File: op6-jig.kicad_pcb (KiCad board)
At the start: 2 copper layers, 75 x 60.6 mm, 43 parts, among them J1 PHONE_TP_BREAKOUT, J2 JTAG_ATMEGA, J3 ATMEGA_MISC_GPIO, P1 USB_C_ATMEGA, P2 USB_C_PHONE, Q1 FQP27P06, SW1 SW_RESET, U1 ATMEGA32U4, U2 LSF0102YZTR, Y1 16MHz

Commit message: PCB: fix missing trace :C
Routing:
- net Net-(R11-Pad2): track 40.5 -> 52.7 mm
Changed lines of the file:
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@@
     (thickness 1.6)
     (drawings 84)
-    (tracks 705)
+    (tracks 709)
     (zones 0)
     (modules 43)
@@
   (segment (start 126.9264 107.409) (end 126.0799 106.5625) (width 0.25) (layer F.Cu) (net 29))
   (segment (start 126.0799 106.5625) (end 126.0799 106.4028) (width 0.25) (layer F.Cu) (net 29))
-  (via (at 126.0799 106.4028) (size 0.8) (layers F.Cu B.Cu) (net 29))
+  (via (at 126.0799 106.4028) (size 0.8) (layers F.Cu B.Cu) (net 29) (status 1000000))
   (via (at 97.5382 95.8206) (size 0.8) (layers F.Cu B.Cu) (net 29))
+  (segment (start 124.422099 104.744999) (end 126.0799 106.4028) (width 0.25) (layer B.Cu) (net 29))
+  (segment (start 121.525997 104.744999) (end 124.422099 104.744999) (width 0.25) (layer B.Cu) (net 29))
+  (segment (start 118.632998 101.852) (end 121.525997 104.744999) (width 0.25) (layer B.Cu) (net 29))
+  (segment (start 115.6776 101.852) (end 118.632998 101.852) (width 0.25) (layer B.Cu) (net 29))
   (via (at 89.4421 104.4869) (size 0.8) (layers F.Cu B.Cu) (net 30))
   (via (at 107.0924 118.3728) (size 0.8) (layers F.Cu B.Cu) (net 30))

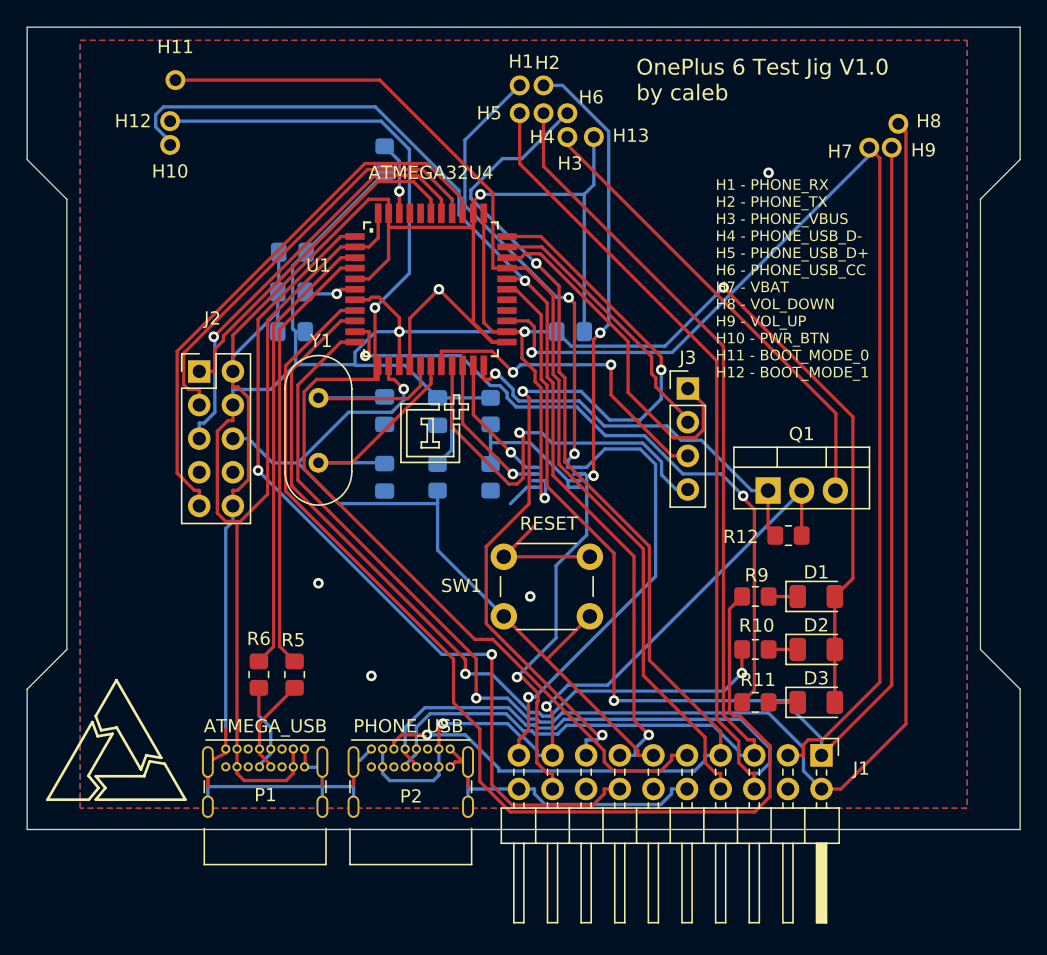
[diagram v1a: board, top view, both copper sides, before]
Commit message: pcb: rewire by hand
hah, i actually did it...

The PCB is now hand wired and muuuuuuuch better. This drops the USB pins
on the breakout header because they probably aren't needed and added too
much complexity to the traces.

Also replace the UART pinout with the 5v one on the Atmega side of the
level shifter rather than the 1.8v levels at the phone.
 * This would mean UART is borked unless you attach 5v to the Atmega USB
   port, maybe we want to power the level shifter with the phone vbus
   supply instead ?
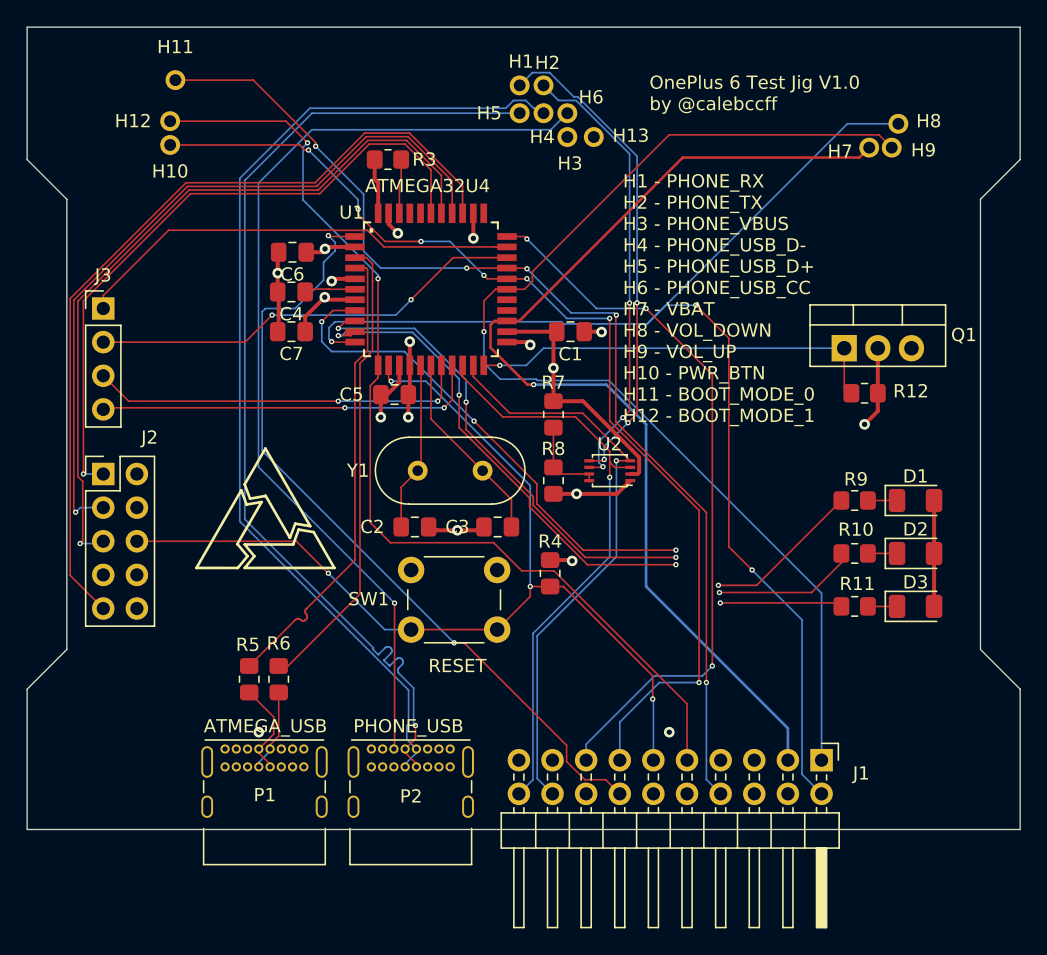
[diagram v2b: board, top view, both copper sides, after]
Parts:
- C1, C2, C3, C4, C5, C6, C7, R3, R4, R7, R8, U2: moved to F.Cu
- H4: value PHONE_USB_DN -> PHONE_USB_D-
- H5: value PHONE_USB_DP -> PHONE_USB_D+
- moved J3 44.6 mm to (77.8, 92.2)
- moved Q1 12.2 mm to (133.7, 95.2)
- moved R12 12.2 mm to (135.2, 98.7)
- moved R4 11.2 mm to (111.5, 112.2)
- moved J2 10.6 mm to (77.8, 104.8)
- moved D1 10.4 mm to (139.1, 106.8)
- moved D2 10.4 mm to (139.1, 110.8)
- moved D3 10.4 mm to (139.1, 114.8)
- moved R10 10.4 mm to (134.5, 110.8)
- moved R11 10.4 mm to (134.5, 114.8)
- moved R9 10.4 mm to (134.5, 106.8)
- moved C3 9.32 mm to (107.5, 108.8), turned to 180 degrees
- moved Y1 9.30 mm to (101.5, 104.5), turned to 0 degrees
- moved C2 9.08 mm to (101.3, 108.8), turned to 0 degrees
- moved SW1 7.07 mm to (101.0, 112.0)
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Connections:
- net Net-(P1-PadA6) renamed /ATMEGA_USB_D-
- net Net-(P1-PadA7) renamed /ATMEGA_USB_D+
- net Net-(R10-Pad2) renamed /LED_G_EN
- net Net-(R11-Pad2) renamed /LEG_B_EN
- net Net-(R5-Pad1) renamed /ATMEGA_USB_R_D-
- net Net-(R6-Pad1) renamed /ATMEGA_USB_R_D+
- net Net-(R9-Pad2) renamed /LED_R_EN
- H4 pad 1: PHONE_USB_DN -> PHONE_USB_D-
- H5 pad 1: PHONE_USB_DP -> PHONE_USB_D+
- J1 pad 18: PHONE_TX -> ATMEGA_TX
- J1 pad 19: PHONE_RX -> GND
- J1 pad 20: GND -> ATMEGA_RX
- J1 pad 5: PHONE_USB_DN -> Net-(J1-Pad5)
- J1 pad 6: PHONE_USB_DP -> Net-(J1-Pad6)
- J1 pad 7: PHONE_USB_CC -> Net-(J1-Pad7)
- P2 pad A6: PHONE_USB_DP -> PHONE_USB_D+
- P2 pad A7: PHONE_USB_DN -> PHONE_USB_D-
- P2 pad B6: PHONE_USB_DP -> PHONE_USB_D+
- P2 pad B7: PHONE_USB_DN -> PHONE_USB_D-
- U1 pad 20: Net-(U1-Pad20) -> ATMEGA_RX
- U1 pad 21: Net-(U1-Pad21) -> ATMEGA_TX
- U1 pad 31: Net-(J3-Pad1) -> Net-(J3-Pad2)
- U1 pad 32: Net-(J3-Pad2) -> Net-(J3-Pad1)
- U2 pad 3: Net-(U1-Pad20) -> ATMEGA_RX
- U2 pad 4: Net-(U1-Pad21) -> ATMEGA_TX
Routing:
- net /5v: track 214.2 -> 55.9 mm, vias 4 -> 6
- net GND: track 195.9 -> 47.7 mm, vias 6 -> 11
- net PHONE_USB_DP: track 95.7 -> 0.00 mm
- net PHONE_USB_DN: track 86.8 -> 0.00 mm
- net PHONE_USB_D+: track 0.00 -> 76.5 mm, vias 0 -> 1
- net PHONE_USB_D-: track 0.00 -> 76.2 mm
- net ATMEGA_RX: track 0.00 -> 44.7 mm, vias 0 -> 1
- net ATMEGA_TX: track 0.00 -> 44.5 mm, vias 0 -> 1
- net /LED_R_EN: track 84.9 -> 50.6 mm, vias 0 -> 4
- net PHONE_RX: track 68.9 -> 37.0 mm
- net PHONE_TX: track 61.6 -> 34.4 mm
- net JTAG_TMS: track 32.5 -> 56.8 mm
- net JTAG_TCK: track 26.2 -> 49.8 mm, vias 0 -> 1
- net JTAG_TCO: track 32.9 -> 55.8 mm, vias 0 -> 1
- net VOL_DOWN: track 119.4 -> 97.5 mm, vias 1 -> 3
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- added copper zone on In2.Cu, net /5v
- added copper zone on In1.Cu, net GND
- removed copper zone on B.Cu, net GND
- removed copper zone on F.Cu, net GND
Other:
- copper layers 2 -> 4
- net class Default: clearance 0.2 -> 0.15; trace_width 0.25 -> 0.127
- net class Power added: clearance 0.15, trace_width 0.3, via_dia 0.8, via_drill 0.4
- net class VBAT added: clearance 0.15, trace_width 0.2, via_dia 0.8, via_drill 0.4
- rule trace_clearance: 0.2 -> 0.15
- rule trace_min: 0.2 -> 0.1
- rule via_min_drill: 0.3 -> 0.2
- board text added: "OnePlus 6 Test Jig V1.0 by @calebccff"
- board text removed: "OnePlus 6 Test Jig V1.0 by caleb"

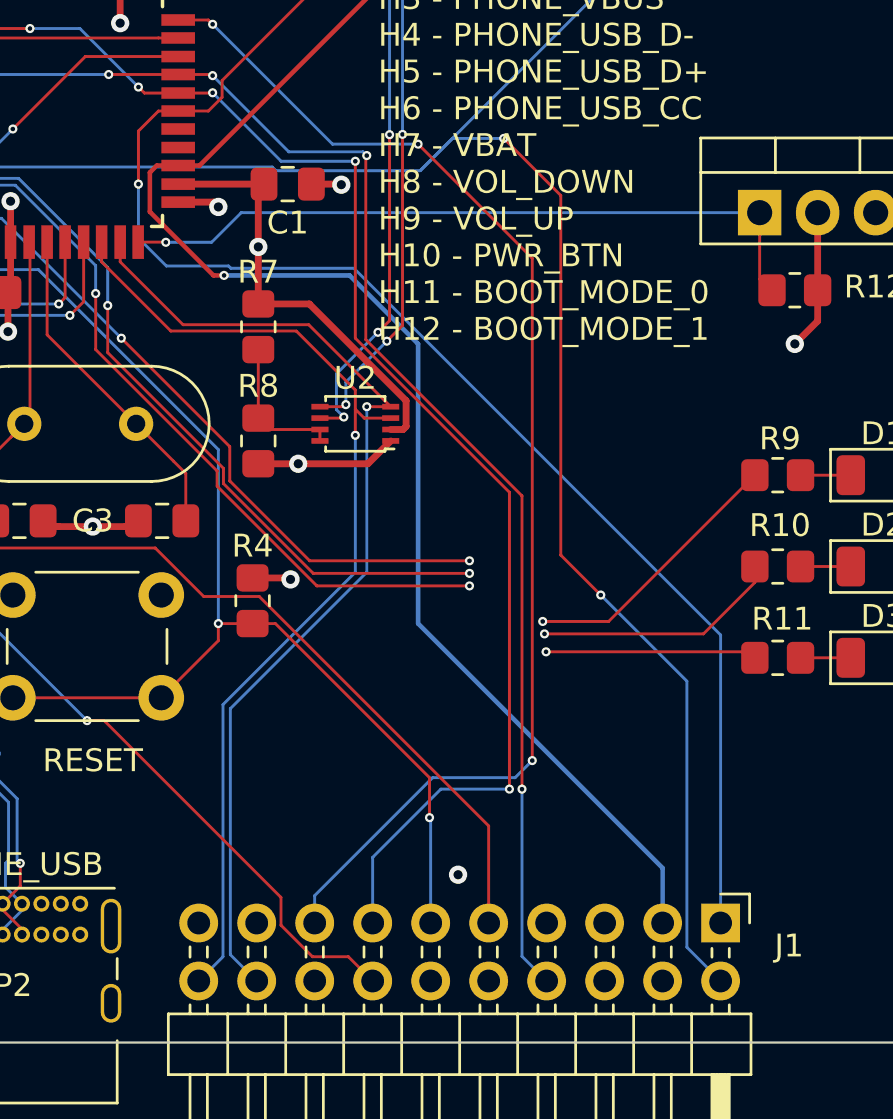
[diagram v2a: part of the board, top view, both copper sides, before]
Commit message: PCB: improve some routing
Less vias = more good :D
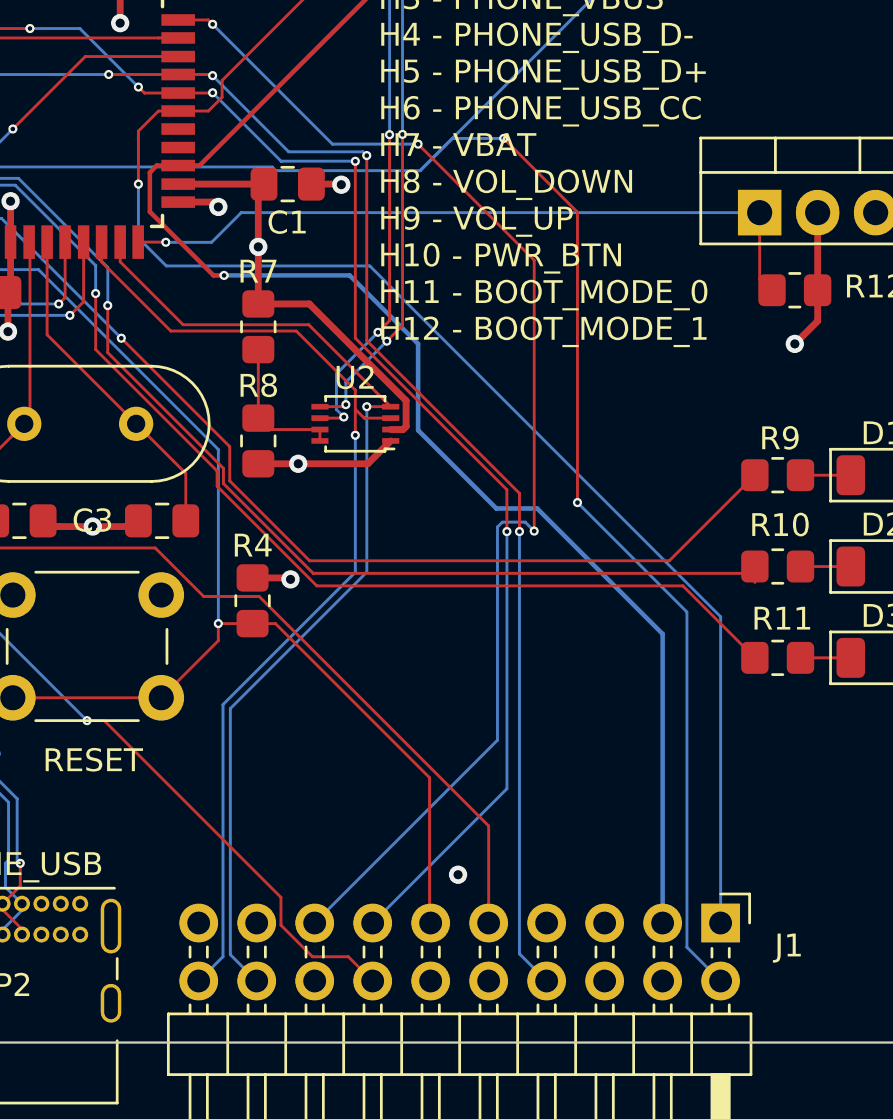
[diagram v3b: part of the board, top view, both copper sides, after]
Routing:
- net /LEG_B_EN: track 46.1 -> 51.0 mm, vias 4 -> 2
- net /LED_G_EN: track 47.7 -> 50.1 mm, vias 4 -> 2
- net /LED_R_EN: track 50.6 -> 52.6 mm, vias 4 -> 2
- net PWR_BTN: track 79.7 -> 77.8 mm
- net VBAT: track 79.8 -> 80.9 mm
- net HWB: track 55.0 -> 54.3 mm
- net RESET: vias 4 -> 3

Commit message: some minor fixes
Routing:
- net /5v: track 55.9 -> 69.1 mm, vias 6 -> 8
- net GND: track 47.7 -> 60.6 mm, vias 11 -> 10

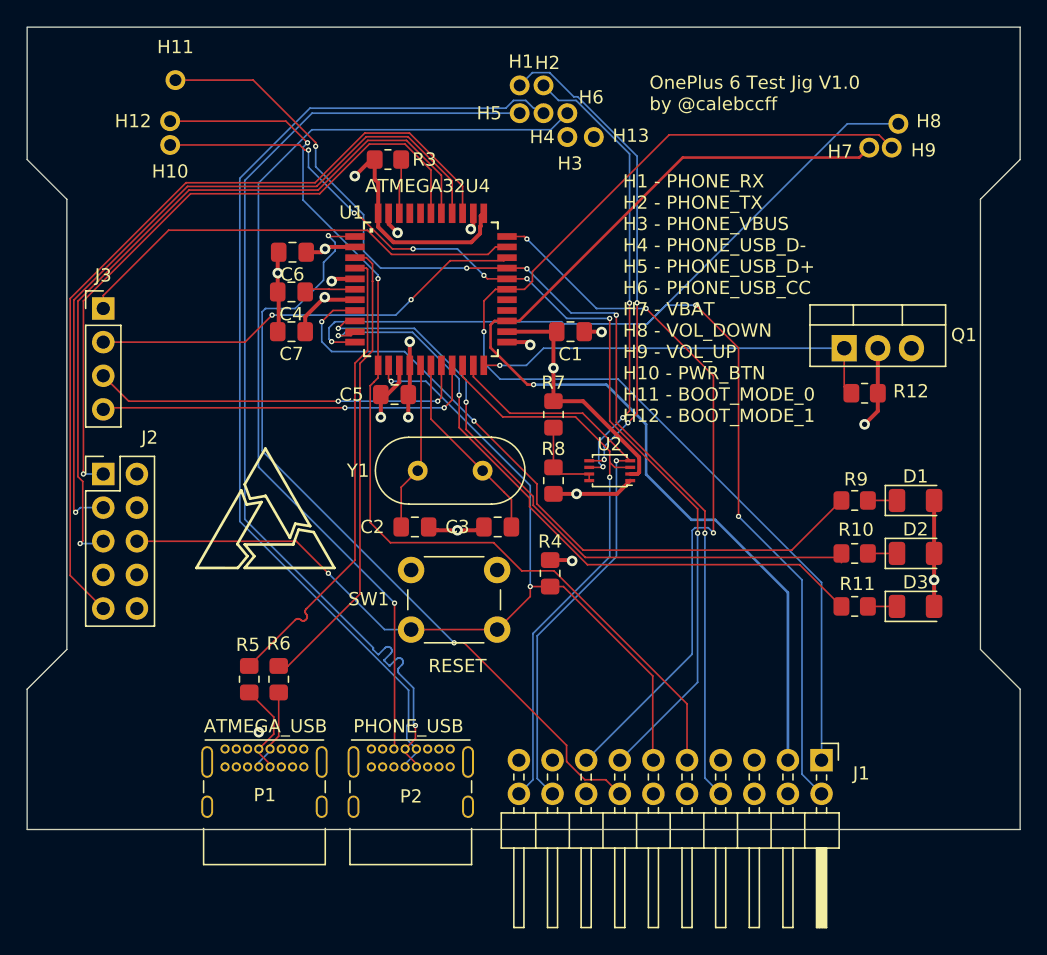
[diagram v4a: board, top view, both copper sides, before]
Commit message: updates, ready-er to produce?
* Replaced the mosfet with a switching IC (thanks @A13).
* Removed ATMEGA MISC header, put those pins on the general 20-pin
  header.
* Replaced USB-C part with a better SMD part (thanks again @A13).
* Some misc fixes / routing improvements.
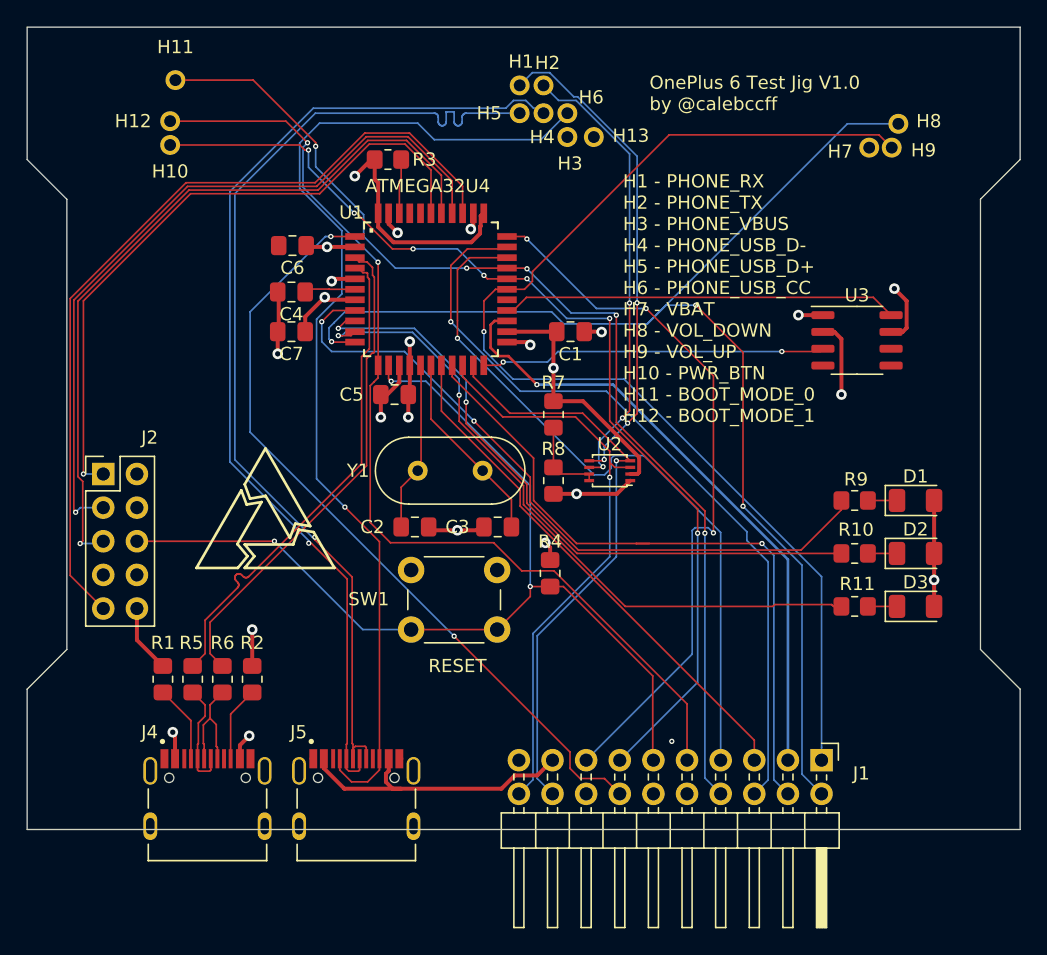
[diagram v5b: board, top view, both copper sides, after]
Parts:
- removed J3: ATMEGA_MISC_GPIO, Connector_PinHeader_2.54mm:PinHeader_1x04_P2.54mm_Vertical
- removed P1: USB_C_ATMEGA, Connector_USB:USB_C_Receptacle_GCT_USB4085
- removed P2: USB_C_PHONE, Connector_USB:USB_C_Receptacle_GCT_USB4085
- removed Q1: FQP27P06, Package_TO_SOT_THT:TO-220-3_Vertical
- removed R12: 10k, Resistor_SMD:R_0805_2012Metric_Pad1.20x1.40mm_HandSolder
- added J4: TYPE-C-31-M-12, Local:HRO_TYPE-C-31-M-12, F.Cu at (85.6, 131.4)
- added J5: TYPE-C-31-M-12, Local:HRO_TYPE-C-31-M-12, F.Cu at (96.9, 131.4)
- added R1: 5.1k, Resistor_SMD:R_0805_2012Metric_Pad1.20x1.40mm_HandSolder, F.Cu at (82.2, 120.2)
- added R2: 5.1k, Resistor_SMD:R_0805_2012Metric_Pad1.20x1.40mm_HandSolder, F.Cu at (89.0, 120.2)
- added U3: AP2192, Package_SO:SO-8_3.9x4.9mm_P1.27mm, F.Cu at (134.7, 94.7)
- C5, C6, C7: value 0.1uF -> 100nF
- R8: value 5k -> 5.6k
- moved R5 4.27 mm to (84.5, 120.2)
- moved R6 4.25 mm to (86.8, 120.2)
- moved C6 0.50 mm to (92.0, 87.5)
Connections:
- J1 pad 12: Net-(J1-Pad12) -> (no net)
- J1 pad 16: Net-(J1-Pad16) -> (no net)
- J1 pad 4: Net-(J1-Pad4) -> ATMEGA_PD1
- J1 pad 5: Net-(J1-Pad5) -> ATMEGA_PD0
- J1 pad 6: Net-(J1-Pad6) -> ATMEGA_PC7
- J1 pad 7: Net-(J1-Pad7) -> ATMEGA_PC6
- J2 pad 7: Net-(J2-Pad7) -> (no net)
- J2 pad 8: Net-(J2-Pad8) -> (no net)
- U1 pad 18: Net-(J3-Pad3) -> ATMEGA_PD0
- U1 pad 19: Net-(J3-Pad4) -> ATMEGA_PD1
- U1 pad 26: Net-(U1-Pad26) -> AP_VBUS_FAULT1
- U1 pad 27: Net-(U1-Pad27) -> (no net)
- U1 pad 31: Net-(J3-Pad2) -> ATMEGA_PC6
- U1 pad 32: Net-(J3-Pad1) -> ATMEGA_PC7
- U1 pad 40: Net-(U1-Pad40) -> (no net)
- U1 pad 41: Net-(U1-Pad41) -> (no net)
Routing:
- net ATMEGA_PC7: track 0.00 -> 58.9 mm, vias 0 -> 1
- net ATMEGA_PC6: track 0.00 -> 54.1 mm, vias 0 -> 1
- net ATMEGA_PD1: track 0.00 -> 52.1 mm, vias 0 -> 1
- net ATMEGA_PD0: track 0.00 -> 39.6 mm
- net Net-(J3-Pad1): track 34.5 -> 0.00 mm
- net Net-(J3-Pad2): track 33.1 -> 0.00 mm, vias 2 -> 0
- net AP_VBUS_FAULT1: track 0.00 -> 30.0 mm
- net Net-(J3-Pad4): track 29.4 -> 0.00 mm, vias 2 -> 0
- net Net-(J3-Pad3): track 28.9 -> 0.00 mm, vias 2 -> 0
- net VBAT: track 80.9 -> 99.6 mm
- net GND: track 60.6 -> 49.4 mm, vias 10 -> 13
- net PHONE_VBUS: track 59.1 -> 65.4 mm
- net VBUS_EN: track 32.2 -> 26.1 mm, vias 1 -> 2
- net Net-(J4-PadA5): track 0.00 -> 5.88 mm
- net Net-(J4-PadB5): track 0.00 -> 5.68 mm
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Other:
- net class Default: clearance 0.15 -> 0.127
- net class VBAT: trace_width 0.2 -> 0.6
- rule trace_clearance: 0.15 -> 0.127
- board text removed: "ATMEGA_USB"
- board text removed: "PHONE_USB"
